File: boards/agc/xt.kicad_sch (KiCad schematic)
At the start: 6 parts, among them Q8 MMBT2222, T11 2:1

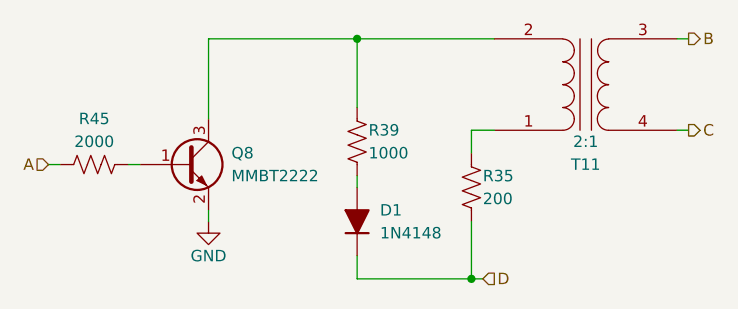
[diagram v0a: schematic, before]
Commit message: Add PSA switching modules and rework fine ref
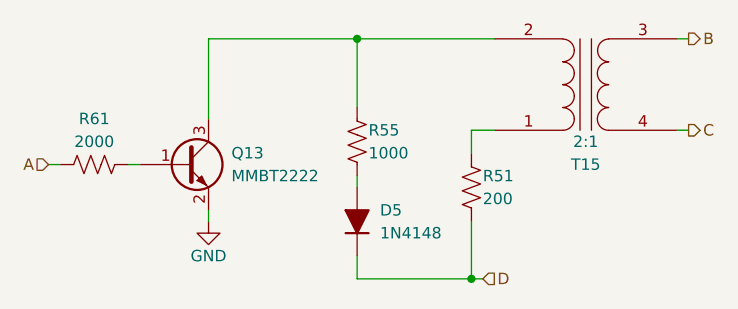
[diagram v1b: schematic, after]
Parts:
- renumbered D1 to D5, Q8 to Q13, R35 to R51, R39 to R55, R45 to R61, T11 to T15
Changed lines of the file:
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@@
 (kicad_sch
-	(version 20231120)
+	(version 20250114)
 	(generator "eeschema")
-	(generator_version "8.0")
+	(generator_version "9.0")
 	(paper "A4")
 	(junction
@@
 		(shape output)
 		(at 130.81 80.01 0)
-		(fields_autoplaced yes)
 		(effects
 			(font
@@
 		(shape input)
 		(at 107.95 106.68 0)
-		(fields_autoplaced yes)
 		(effects
 			(font
@@
 		(shape output)
 		(at 130.81 90.17 0)
-		(fields_autoplaced yes)
 		(effects
 			(font
@@
 		(shape input)
 		(at 59.69 93.98 180)
-		(fields_autoplaced yes)
 		(effects
 			(font
@@
 		(dnp no)
 		(fields_autoplaced yes)
-		(property "Reference" "D1"
+		(property "Reference" "D5"
 			(at 96.52 99.0599 90)
 			(effects
@@
 		(on_board yes)
 		(dnp no)
-		(property "Reference" "R35"
+		(property "Reference" "R51"
 			(at 107.95 95.25 0)
 			(effects
@@
 		(dnp no)
 		(fields_autoplaced yes)
-		(property "Reference" "Q8"
+		(property "Reference" "Q13"
 			(at 80.01 92.7099 0)
 			(effects
@@
 		(on_board yes)
 		(dnp no)
-		(property "Reference" "#PWR019"
+		(property "Reference" "#PWR011"
 			(at 77.47 106.68 0)
 			(effects
@@
 		(on_board yes)
 		(dnp no)
-		(property "Reference" "R45"
+		(property "Reference" "R61"
 			(at 64.77 88.9 90)
 			(effects
@@
 		(on_board yes)
 		(dnp no)
-		(property "Reference" "R39"
+		(property "Reference" "R55"
 			(at 95.25 90.17 0)
 			(effects
@@
 		(on_board yes)
 		(dnp no)
-		(property "Reference" "T11"
+		(property "Reference" "T15"
 			(at 119.38 93.98 0)
 			(effects
